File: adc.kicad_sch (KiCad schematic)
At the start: 15 parts, among them U16001 ADS8665IPWR

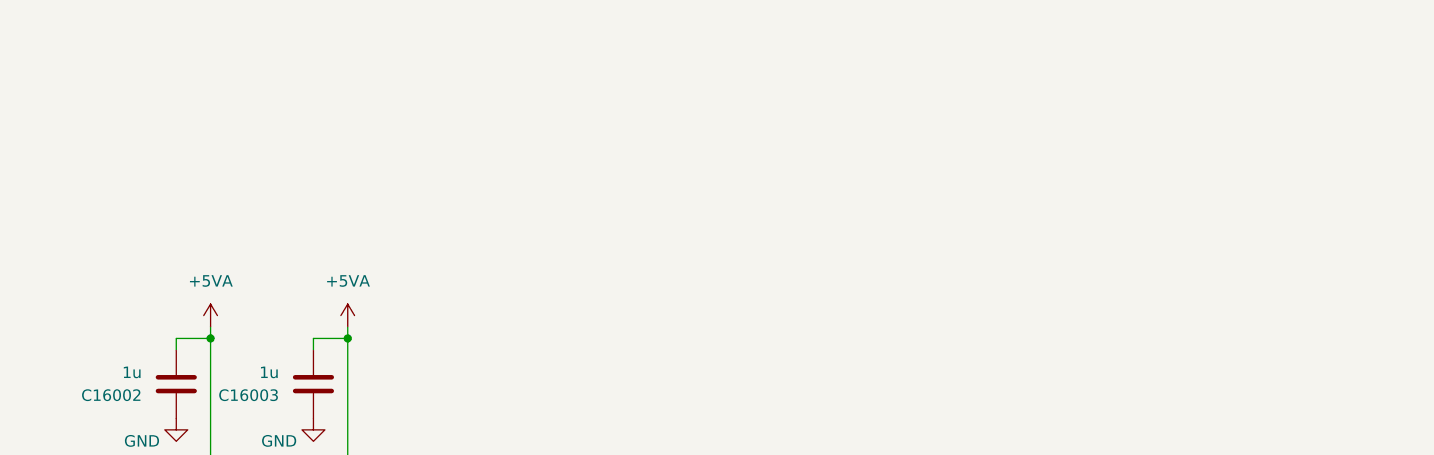
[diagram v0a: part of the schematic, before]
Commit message: edit pss individual power nets for sub circuits
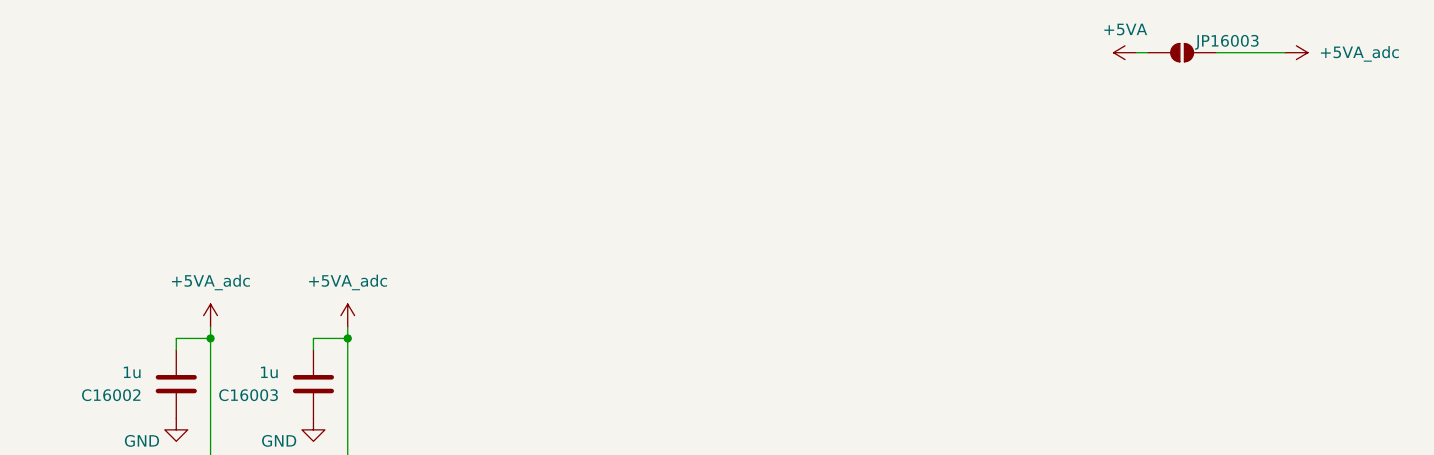
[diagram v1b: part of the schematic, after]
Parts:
- added JP16003: SolderJumper_2_Open, symbol Jumper:SolderJumper_2_Open
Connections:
- net +5VA: now also JP16003.1 (A); no longer C16002.2, C16003.2, JP16001.1 (A), R16001.1, U16001.16 (DVDD), U16001.2 (AVDD)
- new net +5VA_adc: C16002.2, C16003.2, JP16001.1 (A), JP16003.2 (B), R16001.1, U16001.16 (DVDD), U16001.2 (AVDD)

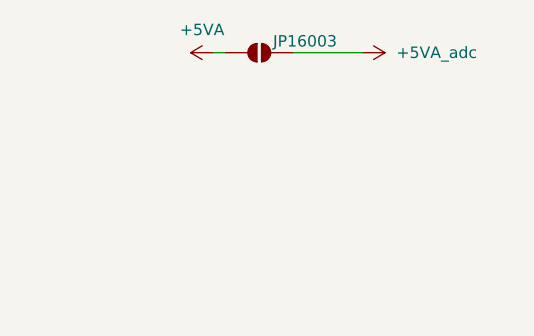
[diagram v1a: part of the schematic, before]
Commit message: fix pss ERC error: missing power flag
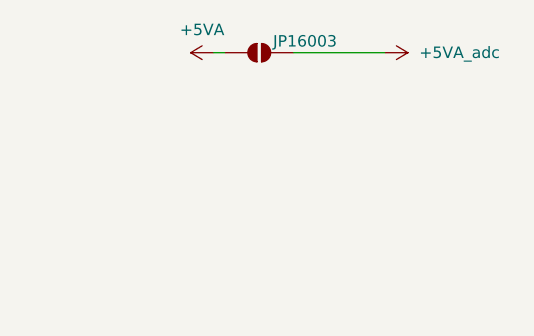
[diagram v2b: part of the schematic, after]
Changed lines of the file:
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@@
 	(wire
 		(pts
-			(xy 248.92 30.48) (xy 241.3 30.48)
+			(xy 241.3 30.48) (xy 251.46 30.48)
 		)
 		(stroke
@@
 	(symbol
 		(lib_id "pss:+5VA_adc")
-		(at 248.92 30.48 270)
+		(at 251.46 30.48 270)
 		(unit 1)
 		(exclude_from_sim no)
@@
 		(fields_autoplaced yes)
 		(property "Reference" "#PWR018007"
-			(at 245.11 30.48 0)
+			(at 247.65 30.48 0)
 			(effects
 				(font
@@
 		)
 		(property "Value" "+5VA_adc"
-			(at 252.73 30.4799 90)
+			(at 255.27 30.4799 90)
 			(effects
 				(font
@@
 		)
 		(property "Footprint" ""
-			(at 248.92 30.48 0)
+			(at 251.46 30.48 0)
 			(effects
 				(font
@@
 		)
 		(property "Datasheet" ""
-			(at 248.92 30.48 0)
+			(at 251.46 30.48 0)
 			(effects
 				(font
@@
 		)
 		(property "Description" ""
-			(at 248.92 30.48 0)
-			(effects
-				(font
+			(at 251.46 30.48 0)
+			(effects
+				(font

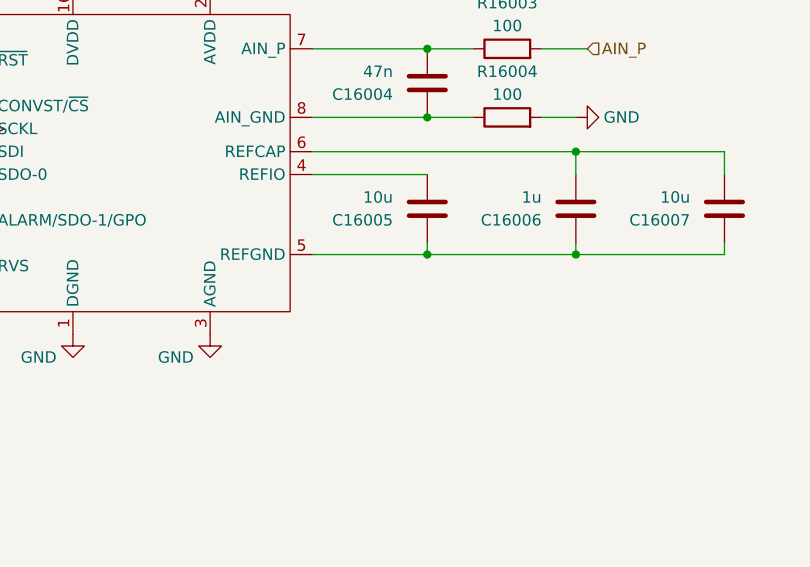
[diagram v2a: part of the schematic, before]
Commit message: fix adc ERC error: missing ground connection for REFGND pin
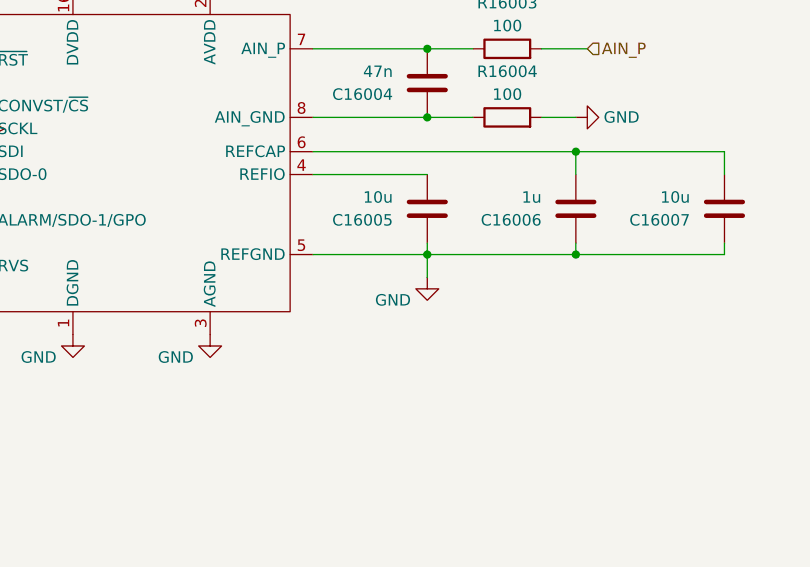
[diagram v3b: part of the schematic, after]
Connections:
- net GND: now also C16005.1, C16006.1, C16007.1, U16001.5 (REFGND)
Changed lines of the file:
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@@
+	(wire
+		(pts
+			(xy 168.91 107.95) (xy 168.91 110.49)
+		)
+		(stroke
+			(width 0)
+			(type default)
+		)
+	)
 	(wire
 		(pts
@@
 					(unit 1)
 				)
+			)
+		)
+	)
+	(symbol
+		(lib_id "pss:GND")
+		(at 168.91 110.49 0)
+		(unit 1)
+		(exclude_from_sim no)
+		(in_bom yes)
+		(on_board yes)
+		(dnp no)
+		(property "Reference" "#PWR016012"
+			(at 168.91 116.84 0)
+			(effects
+				(font
+					(size 1.27 1.27)
+				)
+				(hide yes)
+			)
+		)
+		(property "Value" "GND"
+			(at 165.1 113.03 0)
+			(effects
+				(font
+					(size 1.27 1.27)
+				)
+			)
+		)
+		(property "Footprint" ""
+			(at 168.91 110.49 0)
+			(effects
+				(font
+					(size 1.27 1.27)
+				)
+				(hide yes)
+			)
+		)
+		(property "Datasheet" ""
+			(at 168.91 110.49 0)
+			(effects
+				(font
+					(size 1.27 1.27)
+				)
+				(hide yes)
+			)
+		)
+		(property "Description" "Power symbol creates a global label with name \"GND\" , ground"
+			(at 168.91 110.49 0)
+			(effects
+				(font
+					(size 1.27 1.27)
+				)
+				(hide yes)
+			)
+		)
+		(pin "1"
+		)
+		(instances
+			(project "pss"
+				(path "/3c438cf7-9350-4e9f-8115-1deba8984176/2c843779-6372-445d-93a0-61df61e4217d"
+					(reference "#PWR016012")
+					(unit 1)
+				)
+				(path "/3c438cf7-9350-4e9f-8115-1deba8984176/fe6e657f-8cbe-4801-b8df-4392026dbf94"
+					(reference "#PWR018001")
+					(unit 1)
+				)

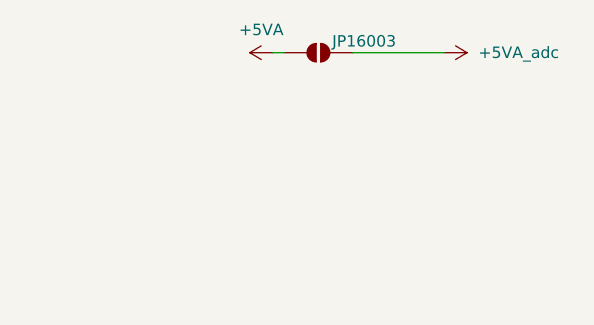
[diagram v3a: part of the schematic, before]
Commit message: fix pss ERC errors: multiple outputs connected
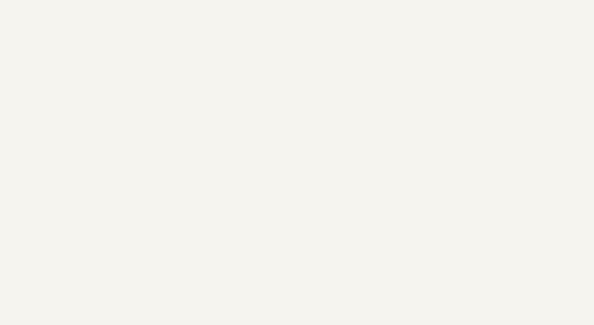
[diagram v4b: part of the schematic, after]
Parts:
- removed JP16003: SolderJumper_2_Open, symbol Jumper:SolderJumper_2_Open
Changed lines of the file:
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@@
+	)
+	(junction
+		(at 185.42 96.52)
+		(diameter 0)
+		(color 0 0 0 0)
+	)
+	(junction
+		(at 88.9 76.2)
+		(diameter 0)
+		(color 0 0 0 0)
 	)
 	(junction
@@
 	)
 	(junction
-		(at 185.42 96.52)
-		(diameter 0)
-		(color 0 0 0 0)
-	)
-	(junction
-		(at 88.9 76.2)
-		(diameter 0)
-		(color 0 0 0 0)
-	)
-	(junction
 		(at 168.91 85.09)
 		(diameter 0)
@@
 	(wire
 		(pts
+			(xy 201.93 99.06) (xy 201.93 96.52)
+		)
+		(stroke
+			(width 0)
+			(type default)
+		)
+	)
+	(wire
+		(pts
+			(xy 129.54 62.23) (xy 125.73 62.23)
+		)
+		(stroke
+			(width 0)
+			(type default)
+		)
+	)
+	(wire
+		(pts
+			(xy 156.21 85.09) (xy 168.91 85.09)
+		)
+		(stroke
+			(width 0)
+			(type default)
+		)
+	)
+	(wire
+		(pts
+			(xy 156.21 92.71) (xy 168.91 92.71)
+		)
+		(stroke
+			(width 0)
+			(type default)
+		)
+	)
+	(wire
+		(pts
+			(xy 88.9 116.84) (xy 88.9 113.03)
+		)
+		(stroke
+			(width 0)
+			(type default)
+		)
+	)
+	(wire
+		(pts
+			(xy 88.9 86.36) (xy 118.11 86.36)
+		)
+		(stroke
+			(width 0)
+			(type default)
+		)
+	)
+	(wire
+		(pts
+			(xy 86.36 86.36) (xy 88.9 86.36)
+		)
+		(stroke
+			(width 0)
+			(type default)
+		)
+	)
+	(wire
+		(pts
+			(xy 76.2 86.36) (xy 76.2 76.2)
+		)
+		(stroke
+			(width 0)
+			(type default)
+		)
+	)
+	(wire
+		(pts
+			(xy 129.54 60.96) (xy 129.54 62.23)
+		)
+		(stroke
+			(width 0)
+			(type default)
+		)
+	)
+	(wire
+		(pts
+			(xy 114.3 99.06) (xy 118.11 99.06)
+		)
+		(stroke
+			(width 0)
+			(type default)
+		)
+	)
+	(wire
+		(pts
+			(xy 156.21 107.95) (xy 168.91 107.95)
+		)
+		(stroke
+			(width 0)
+			(type default)
+		)
+	)
+	(wire
+		(pts
 			(xy 144.78 62.23) (xy 144.78 78.74)
-		)
-		(stroke
-			(width 0)
-			(type default)
-		)
-	)
-	(wire
-		(pts
-			(xy 201.93 99.06) (xy 201.93 96.52)
-		)
-		(stroke
-			(width 0)
-			(type default)
-		)
-	)
-	(wire
-		(pts
-			(xy 129.54 62.23) (xy 125.73 62.23)
-		)
-		(stroke
-			(width 0)
-			(type default)
-		)
-	)
-	(wire
-		(pts
-			(xy 156.21 85.09) (xy 168.91 85.09)
-		)
-		(stroke
-			(width 0)
-			(type default)
-		)
-	)
-	(wire
-		(pts
-			(xy 156.21 92.71) (xy 168.91 92.71)
-		)
-		(stroke
-			(width 0)
-			(type default)
-		)
-	)
-	(wire
-		(pts
-			(xy 88.9 116.84) (xy 88.9 113.03)
-		)
-		(stroke
-			(width 0)
-			(type default)
-		)
-	)
-	(wire
-		(pts
-			(xy 88.9 86.36) (xy 118.11 86.36)
-		)
-		(stroke
-			(width 0)
-			(type default)
-		)
-	)
-	(wire
-		(pts
-			(xy 232.41 30.48) (xy 233.68 30.48)
-		)
-		(stroke
-			(width 0)
-			(type default)
-		)
-	)
-	(wire
-		(pts
-			(xy 86.36 86.36) (xy 88.9 86.36)
-		)
-		(stroke
-			(width 0)
-			(type default)
-		)
-	)
-	(wire
-		(pts
-			(xy 76.2 86.36) (xy 76.2 76.2)
-		)
-		(stroke
-			(width 0)
-			(type default)
-		)
-	)
-	(wire
-		(pts
-			(xy 129.54 60.96) (xy 129.54 62.23)
-		)
-		(stroke
-			(width 0)
-			(type default)
-		)
-	)
-	(wire
-		(pts
-			(xy 114.3 99.06) (xy 118.11 99.06)
-		)
-		(stroke
-			(width 0)
-			(type default)
-		)
-	)
-	(wire
-		(pts
-			(xy 156.21 107.95) (xy 168.91 107.95)
-		)
-		(stroke
-			(width 0)
-			(type default)
-		)
-	)
-	(wire
-		(pts
-			(xy 241.3 30.48) (xy 251.46 30.48)
 		)
 		(stroke
@@
 				(path "/3c438cf7-9350-4e9f-8115-1deba8984176/fe6e657f-8cbe-4801-b8df-4392026dbf94"
 					(reference "#PWR018011")
-					(unit 1)
-				)
-			)
-		)
-	)
-	(symbol
-		(lib_id "power:+5VA")
-		(at 232.41 30.48 90)
-		(unit 1)
-		(exclude_from_sim no)
-		(in_bom yes)
-		(on_board yes)
-		(dnp no)
-		(fields_autoplaced yes)
-		(property "Reference" "#PWR016010"
-			(at 236.22 30.48 0)
-			(effects
-				(font
-					(size 1.27 1.27)
-				)
-				(hide yes)
-			)
-		)
-		(property "Value" "+5VA"
-			(at 231.14 27.94 90)
-			(effects
-				(font
-					(size 1.27 1.27)
-				)
-			)
-		)
-		(property "Footprint" ""
-			(at 232.41 30.48 0)
-			(effects
-				(font
-					(size 1.27 1.27)
-				)
-				(hide yes)
-			)
-		)
-		(property "Datasheet" ""
-			(at 232.41 30.48 0)
-			(effects
-				(font
-					(size 1.27 1.27)
-				)
-				(hide yes)
-			)
-		)
-		(property "Description" "Power symbol creates a global label with name \"+5VA\""
-			(at 232.41 30.48 0)
-			(effects
-				(font
-					(size 1.27 1.27)
-				)
-				(hide yes)
-			)
-		)
-		(pin "1"
-		)
-		(instances
-			(project "pss"
-				(path "/3c438cf7-9350-4e9f-8115-1deba8984176/2c843779-6372-445d-93a0-61df61e4217d"
-					(reference "#PWR016010")
-					(unit 1)
-				)
-				(path "/3c438cf7-9350-4e9f-8115-1deba8984176/fe6e657f-8cbe-4801-b8df-4392026dbf94"
-					(reference "#PWR018013")
 					(unit 1)
 				)
@@
 	)
 	(symbol
-		(lib_id "pss:+5VA_adc")
-		(at 251.46 30.48 270)
-		(unit 1)
-		(exclude_from_sim no)
-		(in_bom yes)
-		(on_board yes)
-		(dnp no)
-		(fields_autoplaced yes)
-		(property "Reference" "#PWR018007"
-			(at 247.65 30.48 0)
-			(effects
-				(font
-					(size 1.27 1.27)
-				)
-				(hide yes)
-			)
-		)
-		(property "Value" "+5VA_adc"
-			(at 255.27 30.4799 90)
-			(effects
-				(font
-					(size 1.27 1.27)
-				)
-				(justify left)
-			)
-		)
-		(property "Footprint" ""
-			(at 251.46 30.48 0)
-			(effects
-				(font
-					(size 1.27 1.27)
-				)
-				(hide yes)
-			)
-		)
-		(property "Datasheet" ""
-			(at 251.46 30.48 0)
-			(effects
-				(font
-					(size 1.27 1.27)
-				)
-				(hide yes)
-			)
-		)
-		(property "Description" ""
-			(at 251.46 30.48 0)
-			(effects
-				(font
-					(size 1.27 1.27)
-				)
-				(hide yes)
-			)
-		)
-		(pin "1"
-		)
-		(instances
-			(project "pss"
-				(path "/3c438cf7-9350-4e9f-8115-1deba8984176/fe6e657f-8cbe-4801-b8df-4392026dbf94"
-					(reference "#PWR018007")
-					(unit 1)
-				)
-				(path "/3c438cf7-9350-4e9f-8115-1deba8984176/2c843779-6372-445d-93a0-61df61e4217d"
-					(reference "#PWR016004")
-					(unit 1)
-				)
-			)
-		)
-	)
-	(symbol
 		(lib_id "pss:GND")
 		(at 88.9 95.25 0)
@@
 					(unit 1)
 				)
-			)
-		)
-	)
-	(symbol
-		(lib_id "Jumper:SolderJumper_2_Open")
-		(at 237.49 30.48 0)
-		(unit 1)
-		(exclude_from_sim yes)
-		(in_bom no)
-		(on_board yes)
-		(dnp no)
-		(property "Reference" "JP16003"
-			(at 242.57 29.21 0)
-			(effects
-				(font
-					(size 1.27 1.27)
-				)
-			)
-		)
-		(property "Value" "SolderJumper_2_Open"
-			(at 212.09 17.78 0)
-			(effects
-				(font
-					(size 1.27 1.27)
-				)
-				(hide yes)
-			)
-		)
-		(property "Footprint" ""
-			(at 237.49 30.48 0)
-			(effects
-				(font
-					(size 1.27 1.27)
-				)
-				(hide yes)
-			)
-		)
-		(property "Datasheet" "~"
-			(at 237.49 30.48 0)
-			(effects
-				(font
-					(size 1.27 1.27)
-				)
-				(hide yes)
-			)
-		)
-		(property "Description" "Solder Jumper, 2-pole, open"
-			(at 237.49 30.48 0)
-			(effects
-				(font
-					(size 1.27 1.27)
-				)
-				(hide yes)
-			)
-		)
-		(pin "1"
-		)
-		(pin "2"
-		)
-		(instances
-			(project "pss"
-				(path "/3c438cf7-9350-4e9f-8115-1deba8984176/2c843779-6372-445d-93a0-61df61e4217d"
-					(reference "JP16003")
-					(unit 1)
-				)
-				(path "/3c438cf7-9350-4e9f-8115-1deba8984176/fe6e657f-8cbe-4801-b8df-4392026dbf94"
-					(reference "JP18003")
-					(unit 1)
-				)
